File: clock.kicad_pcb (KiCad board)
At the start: 2 copper layers, 130 parts, among them J1 USB_C_Receptacle_USB2.0_16P, J3 Conn_01x02_Pin, J5 Battery, Q1 2N7002K, Q2 NPN, U1 STM32F072CBT6, U2 USBLC6-2SC6, U4 MCP73871-2CC, U5 AP2112K-3.3, Y1 8MHz

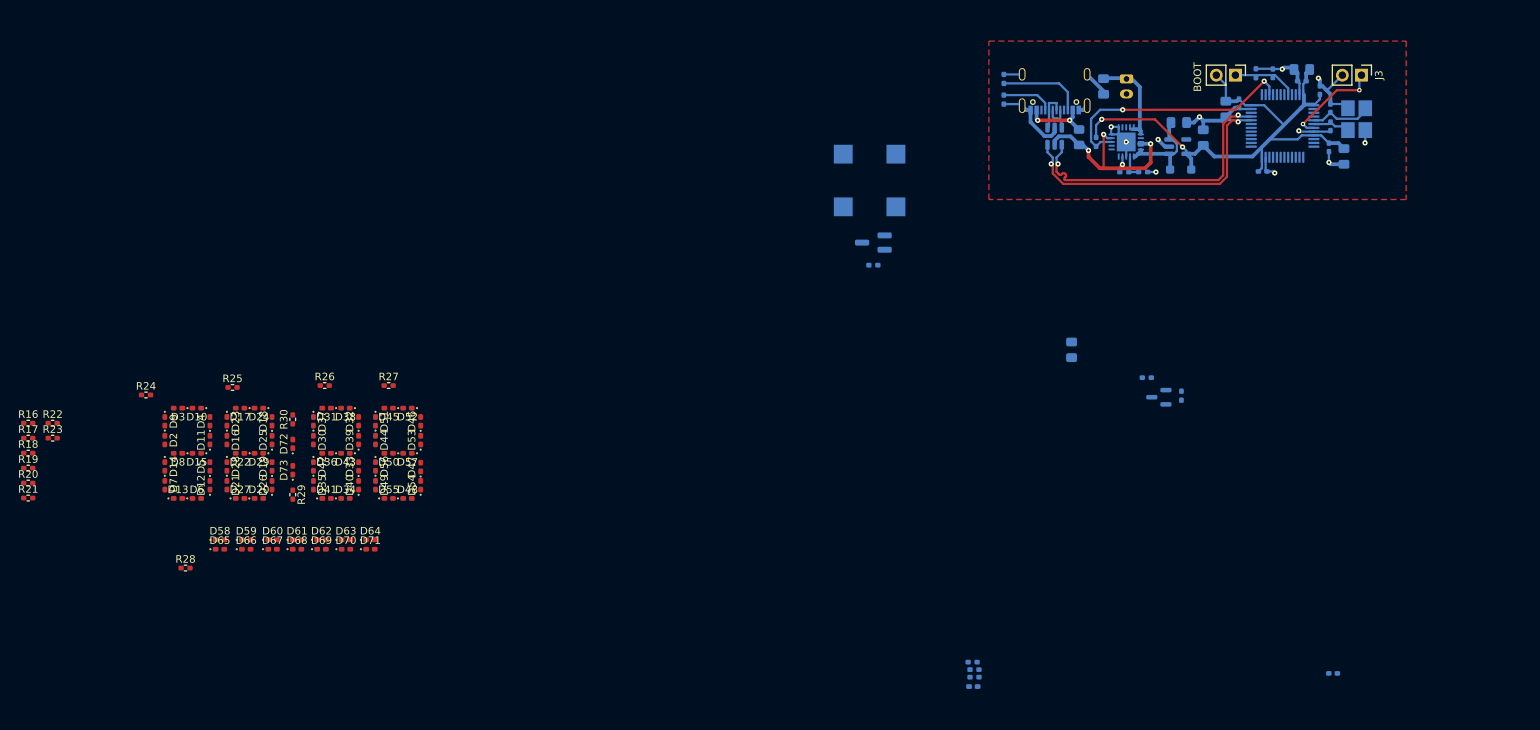
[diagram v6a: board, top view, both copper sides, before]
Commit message: charlie plex routing
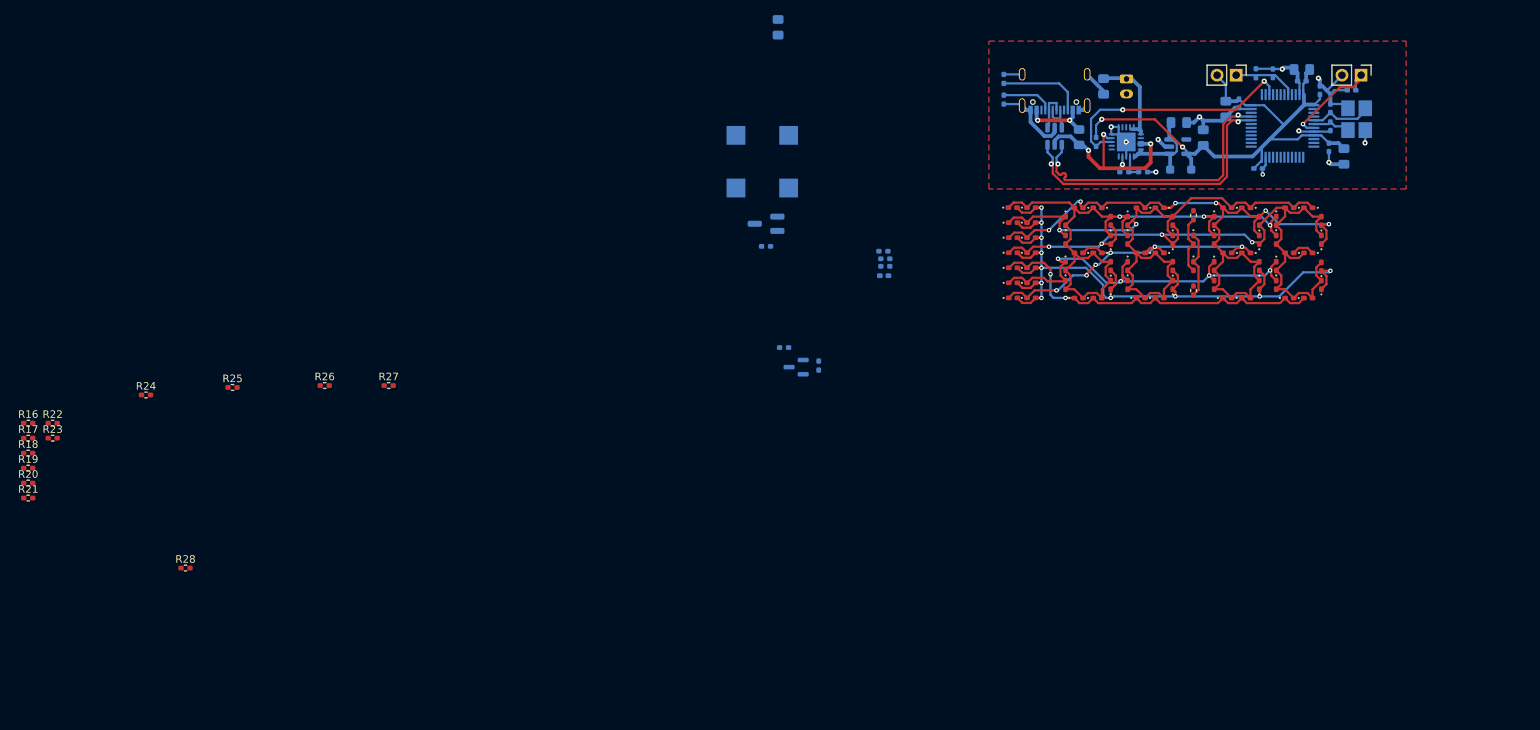
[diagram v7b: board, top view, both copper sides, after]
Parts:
- removed BOOT: Conn_01x02_Pin, Connector_PinHeader_2.54mm:PinHeader_1x02_P2.54mm_Vertical
- added J4: Conn_01x02_Pin, Connector_PinHeader_2.54mm:PinHeader_1x02_P2.54mm_Vertical, F.Cu at (236.9, 28.0)
- moved R29 125.3 mm to (231.2, 46.6), turned to 90 degrees
- moved D73 123.6 mm to (231.2, 49.9), turned to -90 degrees
- moved D10 122.6 mm to (218.4, 45.6)
- moved D11 122.6 mm to (220.2, 49.9)
- moved D12 122.6 mm to (220.2, 55.9)
- moved D13 122.6 mm to (215.9, 57.6)
- moved D14 122.6 mm to (214.2, 53.4)
- moved D15 122.6 mm to (218.4, 51.6)
- moved D16 122.6 mm to (222.4, 49.9)
- moved D17 122.6 mm to (224.2, 45.6)
- moved D18 122.6 mm to (228.4, 47.4)
- moved D19 122.6 mm to (228.4, 53.4)
- moved D2 122.6 mm to (214.2, 49.9)
- moved D20 122.6 mm to (226.7, 57.6)
- moved D21 122.6 mm to (222.4, 55.9)
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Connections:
- D10 pad 1: Net-(D10-K) -> M3
- D10 pad 2: Net-(D10-A) -> M1
- D11 pad 1: Net-(D11-K) -> M4
- D11 pad 2: Net-(D10-A) -> M1
- D12 pad 1: Net-(D12-K) -> M5
- D12 pad 2: Net-(D10-A) -> M1
- D13 pad 1: Net-(D13-K) -> M6
- D13 pad 2: Net-(D10-A) -> M1
- D14 pad 1: Net-(D14-K) -> M7
- D14 pad 2: Net-(D10-A) -> M1
- D15 pad 1: Net-(D15-K) -> M8
- D15 pad 2: Net-(D10-A) -> M1
- D16 pad 1: Net-(D16-K) -> M1
- D16 pad 2: Net-(D16-A) -> M2
- D17 pad 1: Net-(D10-K) -> M3
- D17 pad 2: Net-(D16-A) -> M2
- D18 pad 1: Net-(D11-K) -> M4
- D18 pad 2: Net-(D16-A) -> M2
- D19 pad 1: Net-(D12-K) -> M5
- D19 pad 2: Net-(D16-A) -> M2
- D2 pad 1: Net-(D2-K) -> M2
- D2 pad 2: Net-(D10-A) -> M1
- D20 pad 1: Net-(D13-K) -> M6
- D20 pad 2: Net-(D16-A) -> M2
- D21 pad 1: Net-(D14-K) -> M7
- D21 pad 2: Net-(D16-A) -> M2
- D22 pad 1: Net-(D15-K) -> M8
- D22 pad 2: Net-(D16-A) -> M2
- D23 pad 1: Net-(D16-K) -> M1
- D23 pad 2: Net-(D16-A) -> M2
- D24 pad 1: Net-(D10-K) -> M3
- D24 pad 2: Net-(D16-A) -> M2
- D25 pad 1: Net-(D11-K) -> M4
- D25 pad 2: Net-(D16-A) -> M2
- D26 pad 1: Net-(D12-K) -> M5
- D26 pad 2: Net-(D16-A) -> M2
- D27 pad 1: Net-(D13-K) -> M6
- D27 pad 2: Net-(D16-A) -> M2
- D28 pad 1: Net-(D14-K) -> M7
- D28 pad 2: Net-(D16-A) -> M2
- D29 pad 1: Net-(D15-K) -> M8
- D29 pad 2: Net-(D16-A) -> M2
- D3 pad 1: Net-(D10-K) -> M3
- D3 pad 2: Net-(D10-A) -> M1
- D30 pad 1: Net-(D16-K) -> M1
- D30 pad 2: Net-(D30-A) -> M3
- D31 pad 1: Net-(D2-K) -> M2
- D31 pad 2: Net-(D30-A) -> M3
- D32 pad 1: Net-(D11-K) -> M4
- D32 pad 2: Net-(D30-A) -> M3
- D33 pad 1: Net-(D12-K) -> M5
- D33 pad 2: Net-(D30-A) -> M3
- D34 pad 1: Net-(D13-K) -> M6
- D34 pad 2: Net-(D30-A) -> M3
- D35 pad 1: Net-(D14-K) -> M7
- D35 pad 2: Net-(D30-A) -> M3
- D36 pad 1: Net-(D15-K) -> M8
- D36 pad 2: Net-(D30-A) -> M3
- D37 pad 1: Net-(D16-K) -> M1
- D37 pad 2: Net-(D30-A) -> M3
- D38 pad 1: Net-(D2-K) -> M2
- D38 pad 2: Net-(D30-A) -> M3
- D39 pad 1: Net-(D11-K) -> M4
- D39 pad 2: Net-(D30-A) -> M3
- D4 pad 1: Net-(D11-K) -> M4
- D4 pad 2: Net-(D10-A) -> M1
- D40 pad 1: Net-(D12-K) -> M5
- D40 pad 2: Net-(D30-A) -> M3
- D41 pad 1: Net-(D13-K) -> M6
- D41 pad 2: Net-(D30-A) -> M3
- D42 pad 1: Net-(D14-K) -> M7
- D42 pad 2: Net-(D30-A) -> M3
- D43 pad 1: Net-(D15-K) -> M8
- D43 pad 2: Net-(D30-A) -> M3
- D44 pad 1: Net-(D16-K) -> M1
- D44 pad 2: Net-(D44-A) -> M4
- D45 pad 1: Net-(D2-K) -> M2
- D45 pad 2: Net-(D44-A) -> M4
- D46 pad 1: Net-(D10-K) -> M3
- D46 pad 2: Net-(D44-A) -> M4
- D47 pad 1: Net-(D12-K) -> M5
- D47 pad 2: Net-(D44-A) -> M4
- D48 pad 1: Net-(D13-K) -> M6
- D48 pad 2: Net-(D44-A) -> M4
- D49 pad 1: Net-(D14-K) -> M7
- D49 pad 2: Net-(D44-A) -> M4
- D5 pad 1: Net-(D12-K) -> M5
- D5 pad 2: Net-(D10-A) -> M1
- D50 pad 1: Net-(D15-K) -> M8
- D50 pad 2: Net-(D44-A) -> M4
- D51 pad 1: Net-(D16-K) -> M1
- D51 pad 2: Net-(D44-A) -> M4
- D52 pad 1: Net-(D2-K) -> M2
- D52 pad 2: Net-(D44-A) -> M4
- D53 pad 1: Net-(D10-K) -> M3
- D53 pad 2: Net-(D44-A) -> M4
- D54 pad 1: Net-(D12-K) -> M5
- D54 pad 2: Net-(D44-A) -> M4
- D55 pad 1: Net-(D13-K) -> M6
- D55 pad 2: Net-(D44-A) -> M4
- D56 pad 1: Net-(D14-K) -> M7
- D56 pad 2: Net-(D44-A) -> M4
- D57 pad 1: Net-(D15-K) -> M8
- D57 pad 2: Net-(D44-A) -> M4
- D58 pad 1: Net-(D16-K) -> M1
- D58 pad 2: Net-(D58-A) -> M5
- D59 pad 1: Net-(D2-K) -> M2
- D59 pad 2: Net-(D58-A) -> M5
- D6 pad 1: Net-(D13-K) -> M6
- D6 pad 2: Net-(D10-A) -> M1
- D60 pad 1: Net-(D10-K) -> M3
- D60 pad 2: Net-(D58-A) -> M5
- D61 pad 1: Net-(D11-K) -> M4
- D61 pad 2: Net-(D58-A) -> M5
- D62 pad 1: Net-(D13-K) -> M6
- D62 pad 2: Net-(D58-A) -> M5
- D63 pad 1: Net-(D14-K) -> M7
- D63 pad 2: Net-(D58-A) -> M5
- D64 pad 1: Net-(D15-K) -> M8
- D64 pad 2: Net-(D58-A) -> M5
- D65 pad 1: Net-(D16-K) -> M1
- D65 pad 2: Net-(D58-A) -> M5
- D66 pad 1: Net-(D2-K) -> M2
- D66 pad 2: Net-(D58-A) -> M5
- D67 pad 1: Net-(D10-K) -> M3
- D67 pad 2: Net-(D58-A) -> M5
- D68 pad 1: Net-(D11-K) -> M4
- D68 pad 2: Net-(D58-A) -> M5
- D69 pad 1: Net-(D13-K) -> M6
- D69 pad 2: Net-(D58-A) -> M5
- D7 pad 1: Net-(D14-K) -> M7
- D7 pad 2: Net-(D10-A) -> M1
- D70 pad 1: Net-(D14-K) -> M7
- D70 pad 2: Net-(D58-A) -> M5
- D71 pad 1: Net-(D15-K) -> M8
- D71 pad 2: Net-(D58-A) -> M5
- D8 pad 1: Net-(D15-K) -> M8
- D8 pad 2: Net-(D10-A) -> M1
- D9 pad 1: Net-(D2-K) -> M2
- D9 pad 2: Net-(D10-A) -> M1
- R16 pad 2: Net-(D16-K) -> M1
- R17 pad 2: Net-(D2-K) -> M2
- R18 pad 2: Net-(D10-K) -> M3
- R19 pad 2: Net-(D11-K) -> M4
- R20 pad 2: Net-(D12-K) -> M5
- R21 pad 2: Net-(D13-K) -> M6
- R22 pad 2: Net-(D14-K) -> M7
- R23 pad 2: Net-(D15-K) -> M8
- R24 pad 2: Net-(D10-A) -> M1
- R25 pad 2: Net-(D16-A) -> M2
- R26 pad 2: Net-(D30-A) -> M3
- R27 pad 2: Net-(D44-A) -> M4
- R28 pad 2: Net-(D58-A) -> M5
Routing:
- net M5: track 0.00 -> 97.5 mm, vias 0 -> 11
- net M4: track 0.00 -> 89.1 mm, vias 0 -> 4
- net M3: track 0.00 -> 88.2 mm, vias 0 -> 6
- net M2: track 0.00 -> 84.7 mm, vias 0 -> 2
- net M1: track 0.00 -> 83.0 mm, vias 0 -> 3
- net M7: track 0.00 -> 53.1 mm, vias 0 -> 4
- net M8: track 0.00 -> 47.9 mm, vias 0 -> 6
- net M6: track 0.00 -> 47.9 mm, vias 0 -> 2
- net Net-(D72-K): track 0.00 -> 9.03 mm
- net Net-(D72-A): track 0.00 -> 7.84 mm
- net GND: track 70.3 -> 72.2 mm
- net NRST: track 13.1 -> 14.7 mm, vias 2 -> 1
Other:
- board text added: "BOOT"
- board text added: "NRST"

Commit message: buttons in place + missing M8 connection
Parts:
- added SW1: SW_SPST, FB_clock_lib:SW_push, F.Cu at (254.8, 51.4)
- added SW2: SW_SPST, FB_clock_lib:SW_push, F.Cu at (254.8, 46.8)
- added SW5: SW_SPST, FB_clock_lib:SW_push, F.Cu at (254.8, 56.0)
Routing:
- net GND: track 72.2 -> 114.8 mm, vias 11 -> 15
- net M8: track 47.9 -> 56.0 mm, vias 6 -> 7
